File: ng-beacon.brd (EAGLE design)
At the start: 71.1 x 76.2 mm, 4 parts

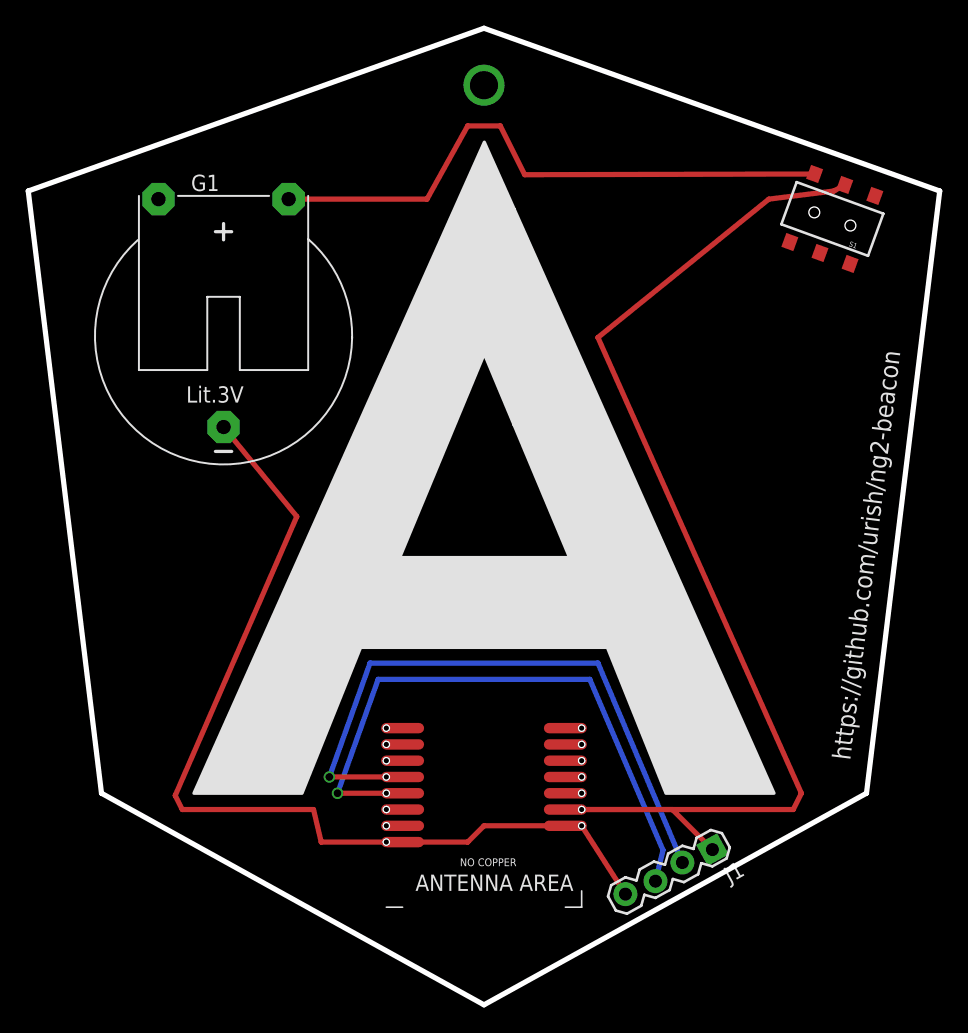
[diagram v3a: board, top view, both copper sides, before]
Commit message: add temperature sensor
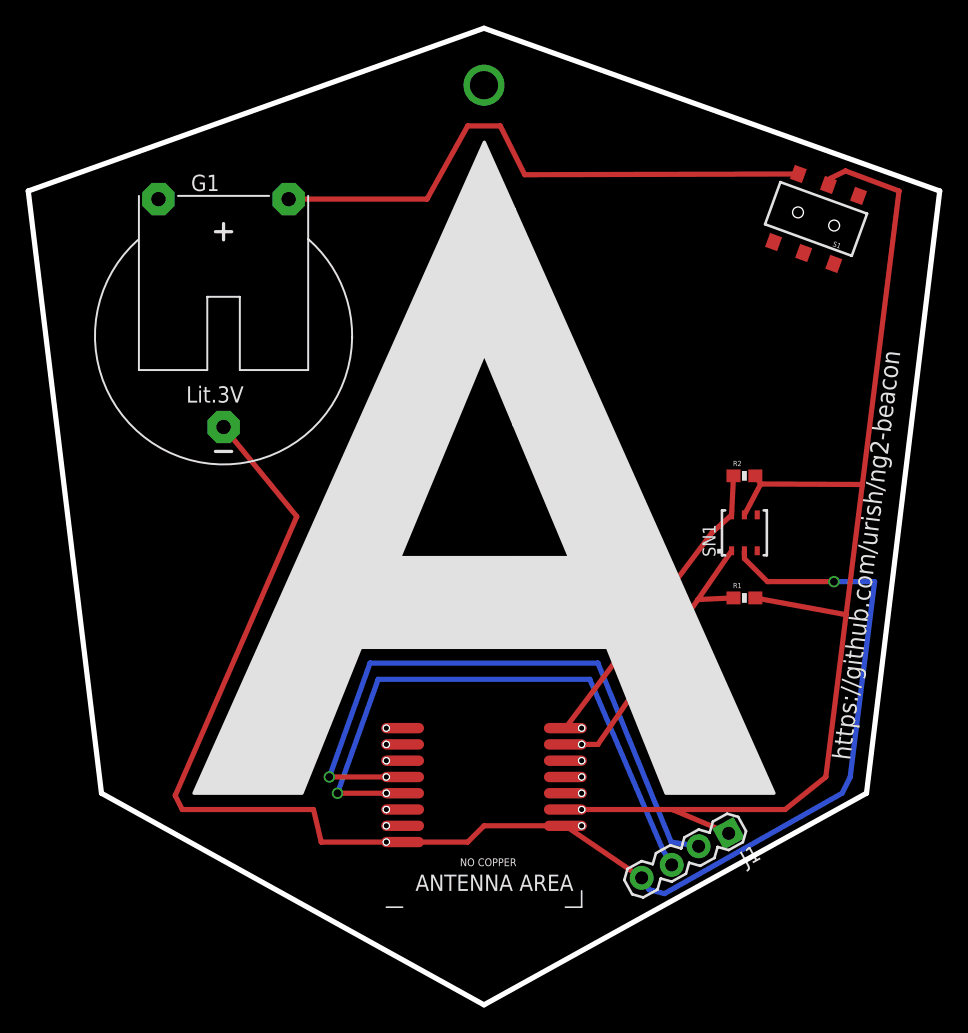
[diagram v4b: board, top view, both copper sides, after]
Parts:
- added R1, R2: 10K, SparkFun-Resistors:0603-RES
- added SN1: SHT21, sensirion:DFN6/SHT
- moved J1 1.80 mm to (64.8, 12.2)
- moved S1 1.27 mm to (71.6, 60.0)
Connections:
- new net SCL: R2.1, SN1.6, U$1.15
- new net SDA: R1.1, SN1.1, U$1.14
- net GND: now also SN1.2
- net VIN: now also R1.2, R2.2, SN1.5
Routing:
- net GND: track 74.0 -> 120.2 mm, vias 0 -> 1
- net SCL: track 0.00 -> 24.2 mm
- net SDA: track 0.00 -> 23.7 mm
- net VIN: track 94.2 -> 97.0 mm
- net N$1: track 46.8 -> 45.5 mm
- net SWCLK: track 48.0 -> 46.9 mm
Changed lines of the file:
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@@
 <element name="G1" library="battery" package="CR2032H" value="CR2032H" x="25.4" y="50.8"/>
 <element name="U$1" library="PTR5518" package="PTR5518" value="PTR5518STD" x="45.72" y="13.97" rot="R180"/>
-<element name="S1" library="SparkFun-Electromechanical" package="AYZ0202" value="DPDT" x="72.900953125" y="60.047775" rot="R160">
-<attribute name="PROD_ID" value="SWCH-08179" x="72.900953125" y="60.047775" size="1.778" layer="27" rot="R160" display="off"/>
+<element name="S1" library="SparkFun-Electromechanical" package="AYZ0202" value="DPDT" x="71.630953125" y="60.047775" rot="R160">
+<attribute name="PROD_ID" value="SWCH-08179" x="71.630953125" y="60.047775" size="1.778" layer="27" rot="R160" display="off"/>
 </element>
-<element name="J1" library="SparkFun-Connectors" package="1X04_LOCK" value="" x="63.48070625" y="10.954234375" rot="R209">
-<attribute name="PROD_ID" value="CONN-09696" x="63.48070625" y="10.954234375" size="1.778" layer="27" rot="R209" display="off"/>
+<element name="J1" library="SparkFun-Connectors" package="1X04_LOCK" value="" x="64.75070625" y="12.224234375" rot="R209">
+<attribute name="PROD_ID" value="CONN-09696" x="64.75070625" y="12.224234375" size="1.778" layer="27" rot="R209" display="off"/>
+</element>
+<element name="SN1" library="sensirion" package="DFN6/SHT" value="SHT21" x="66.04" y="35.56"/>
+<element name="R1" library="SparkFun-Resistors" package="0603-RES" value="10K" x="66.04" y="30.48">
+<attribute name="PROD_ID" value="RES-00824" x="66.04" y="30.48" size="1.778" layer="27" display="off"/>
+</element>
+<element name="R2" library="SparkFun-Resistors" package="0603-RES" value="10K" x="66.04" y="40.005">
+<attribute name="PROD_ID" value="RES-00824" x="66.04" y="40.005" size="1.778" layer="27" display="off"/>
 </element>
 </elements>
@@
 <wire x1="45.72" y1="12.7" x2="52.07" y2="12.7" width="0.4064" layer="1"/>
 <contactref element="J1" pad="4"/>
-<wire x1="56.75453125" y1="7.371059375" x2="53.34" y2="12.7" width="0.4064" layer="1"/>
-<wire x1="53.34" y1="12.7" x2="52.07" y2="12.7" width="0.4064" layer="1"/>
+<contactref element="SN1" pad="2"/>
+<wire x1="52.07" y1="12.7" x2="58.02453125" y2="8.641059375" width="0.4064" layer="1"/>
+<wire x1="66.04" y1="34.16" x2="66.04" y2="33.54605" width="0.4064" layer="1"/>
+<wire x1="66.04" y1="33.54605" x2="67.83605" y2="31.75" width="0.4064" layer="1"/>
+<wire x1="67.83605" y1="31.75" x2="73.025" y2="31.75" width="0.4064" layer="1"/>
+<via x="73.025" y="31.75" extent="1-16" drill="0.6" shape="square"/>
+<wire x1="73.025" y1="31.75" x2="76.2" y2="31.75" width="0.4064" layer="16"/>
+<wire x1="76.2" y1="31.75" x2="74.295" y2="16.51" width="0.4064" layer="16"/>
+<wire x1="74.295" y1="16.51" x2="73.66" y2="15.24" width="0.4064" layer="16"/>
+<wire x1="73.66" y1="15.24" x2="59.8045" y2="7.40863125" width="0.4064" layer="16"/>
+<wire x1="59.8045" y1="7.40863125" x2="58.600153125" y2="7.71598125" width="0.4064" layer="16"/>
+<wire x1="58.600153125" y1="7.71598125" x2="58.02453125" y2="8.641059375" width="0.4064" layer="16"/>
 </signal>
 <signal name="N$1">
@@
 <wire x1="44.45" y1="67.31" x2="46.99" y2="67.31" width="0.4064" layer="1"/>
 <wire x1="46.99" y1="67.31" x2="48.895" y2="63.5" width="0.4064" layer="1"/>
-<wire x1="48.895" y1="63.5" x2="71.517928125" y2="63.55745625" width="0.4064" layer="1"/>
+<wire x1="48.895" y1="63.5" x2="70.247928125" y2="63.55745625" width="0.4064" layer="1"/>
 </signal>
 <signal name="VIN">
 <contactref element="S1" pad="5"/>
 <contactref element="U$1" pad="10"/>
-<wire x1="67.945" y1="61.595" x2="54.61" y2="50.8" width="0.4064" layer="1"/>
-<wire x1="54.61" y1="50.8" x2="70.485" y2="15.24" width="0.4064" layer="1"/>
-<wire x1="70.485" y1="15.24" x2="69.85" y2="13.97" width="0.4064" layer="1"/>
-<wire x1="69.85" y1="13.97" x2="52.07" y2="13.97" width="0.4064" layer="1"/>
-<wire x1="73.867159375" y1="62.70240625" x2="73.025" y2="62.23" width="0.4064" layer="1"/>
-<wire x1="73.025" y1="62.23" x2="67.945" y2="61.595" width="0.4064" layer="1"/>
 <contactref element="J1" pad="1"/>
 <wire x1="52.07" y1="13.97" x2="60.41543125" y2="13.97" width="0.4064" layer="1"/>
-<wire x1="60.41543125" y1="13.97" x2="63.542275" y2="10.84315625" width="0.4064" layer="1"/>
+<wire x1="60.41543125" y1="13.97" x2="64.812275" y2="12.11315625" width="0.4064" layer="1"/>
+<contactref element="SN1" pad="5"/>
+<wire x1="60.41543125" y1="13.97" x2="69.215" y2="13.97" width="0.4064" layer="1"/>
+<wire x1="69.215" y1="13.97" x2="72.39" y2="16.51" width="0.4064" layer="1"/>
+<wire x1="72.39" y1="16.51" x2="73.972615625" y2="29.170921875" width="0.4064" layer="1"/>
+<wire x1="73.972615625" y1="29.170921875" x2="75.242615625" y2="39.330921875" width="0.4064" layer="1"/>
+<wire x1="75.242615625" y1="39.330921875" x2="78.105" y2="62.23" width="0.4064" layer="1"/>
+<wire x1="78.105" y1="62.23" x2="73.9255625" y2="63.7972875" width="0.4064" layer="1"/>
+<wire x1="73.9255625" y1="63.7972875" x2="72.749771875" y2="63.21341875" width="0.4064" layer="1"/>
+<wire x1="72.749771875" y1="63.21341875" x2="72.597159375" y2="62.70240625" width="0.4064" layer="1"/>
+<wire x1="66.04" y1="36.96" x2="67.31" y2="39.37" width="0.4064" layer="1"/>
+<wire x1="67.31" y1="39.37" x2="75.242615625" y2="39.330921875" width="0.4064" layer="1"/>
+<contactref element="R1" pad="2"/>
+<contactref element="R2" pad="2"/>
+<wire x1="66.89" y1="30.48" x2="73.972615625" y2="29.170921875" width="0.4064" layer="1"/>
+<wire x1="66.89" y1="40.005" x2="67.31" y2="39.37" width="0.4064" layer="1"/>
 </signal>
 <signal name="SWCLK">
 <contactref element="J1" pad="3"/>
 <contactref element="U$1" pad="5"/>
-<wire x1="59.09920625" y1="8.380321875" x2="59.69" y2="10.795" width="0.4064" layer="16"/>
+<wire x1="60.36920625" y1="9.650321875" x2="59.69" y2="10.795" width="0.4064" layer="16"/>
 <wire x1="59.69" y1="10.795" x2="53.975" y2="24.13" width="0.4064" layer="16"/>
 <wire x1="53.975" y1="24.13" x2="37.465" y2="24.13" width="0.4064" layer="16"/>
@@
 <contactref element="J1" pad="2"/>
 <contactref element="U$1" pad="4"/>
-<wire x1="61.1976" y1="9.83389375" x2="54.61" y2="25.4" width="0.4064" layer="16"/>
 <wire x1="54.61" y1="25.4" x2="36.83" y2="25.4" width="0.4064" layer="16"/>
 <wire x1="36.83" y1="25.4" x2="33.655" y2="16.51" width="0.4064" layer="16"/>
 <via x="33.655" y="16.51" extent="1-16" drill="0.6" shape="square"/>
 <wire x1="33.655" y1="16.51" x2="39.37" y2="16.51" width="0.4064" layer="1"/>
+<wire x1="54.61" y1="25.4" x2="60.325" y2="11.43" width="0.4064" layer="16"/>
+<wire x1="60.325" y1="11.43" x2="62.4676" y2="11.10389375" width="0.4064" layer="16"/>
+</signal>
+<signal name="SDA">
+<contactref element="U$1" pad="14"/>
+<contactref element="SN1" pad="1"/>
+<wire x1="65.04" y1="34.16" x2="62.412734375" y2="30.353865625" width="0.4064" layer="1"/>
+<wire x1="62.412734375" y1="30.353865625" x2="54.61" y2="19.05" width="0.4064" layer="1"/>
+<wire x1="54.61" y1="19.05" x2="52.07" y2="19.05" width="0.4064" layer="1"/>
+<contactref element="R1" pad="1"/>
+<wire x1="65.19" y1="30.48" x2="62.412734375" y2="30.353865625" width="0.4064" layer="1"/>
+</signal>
+<signal name="SCL">
+<contactref element="U$1" pad="15"/>
+<contactref element="SN1" pad="6"/>
+<wire x1="65.04" y1="36.96" x2="63.5" y2="35.56" width="0.4064" layer="1"/>
+<wire x1="63.5" y1="35.56" x2="52.07" y2="20.32" width="0.4064" layer="1"/>
+<contactref element="R2" pad="1"/>
+<wire x1="65.19" y1="40.005" x2="65.04" y2="36.96" width="0.4064" layer="1"/>
+</signal>
+<signal name="N$2">
 </signal>
 </signals>
